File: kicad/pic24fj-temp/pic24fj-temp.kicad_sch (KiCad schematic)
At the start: 18 parts, among them Q1 BC328, Q2 BC328, Q3 BC328, Q4 BC328, U2 CA56-12CGKWA

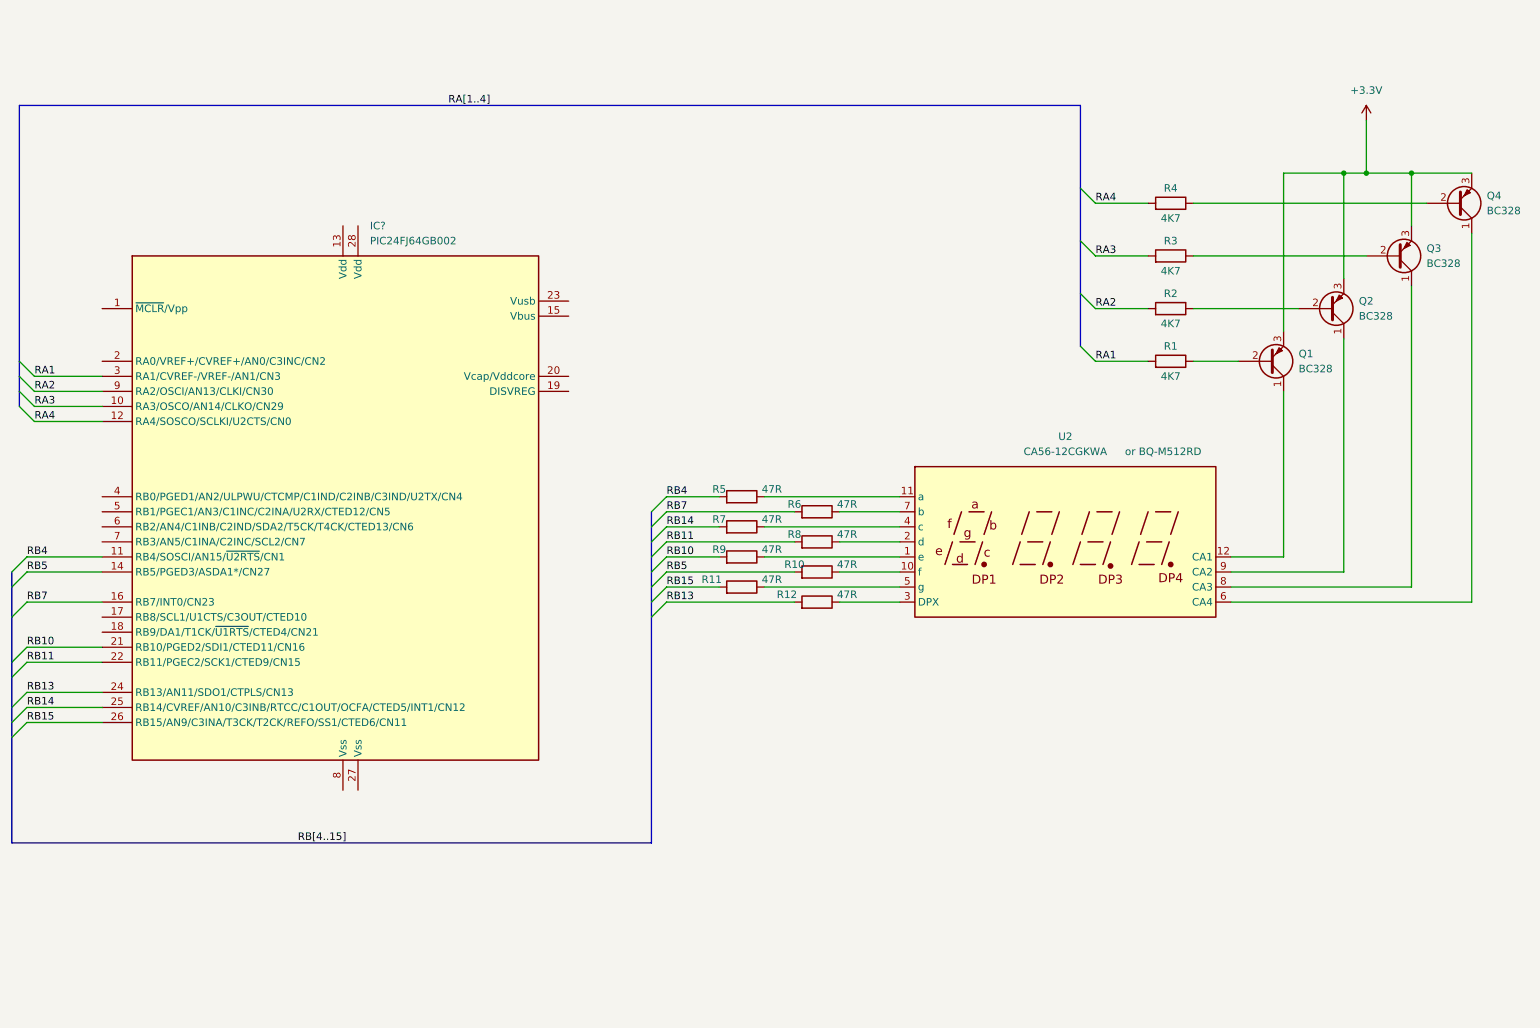
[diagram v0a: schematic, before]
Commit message: Added DS18B20 (no code yet), increased Mux freq from 100 Hz to 200 Hz to reduce flicker
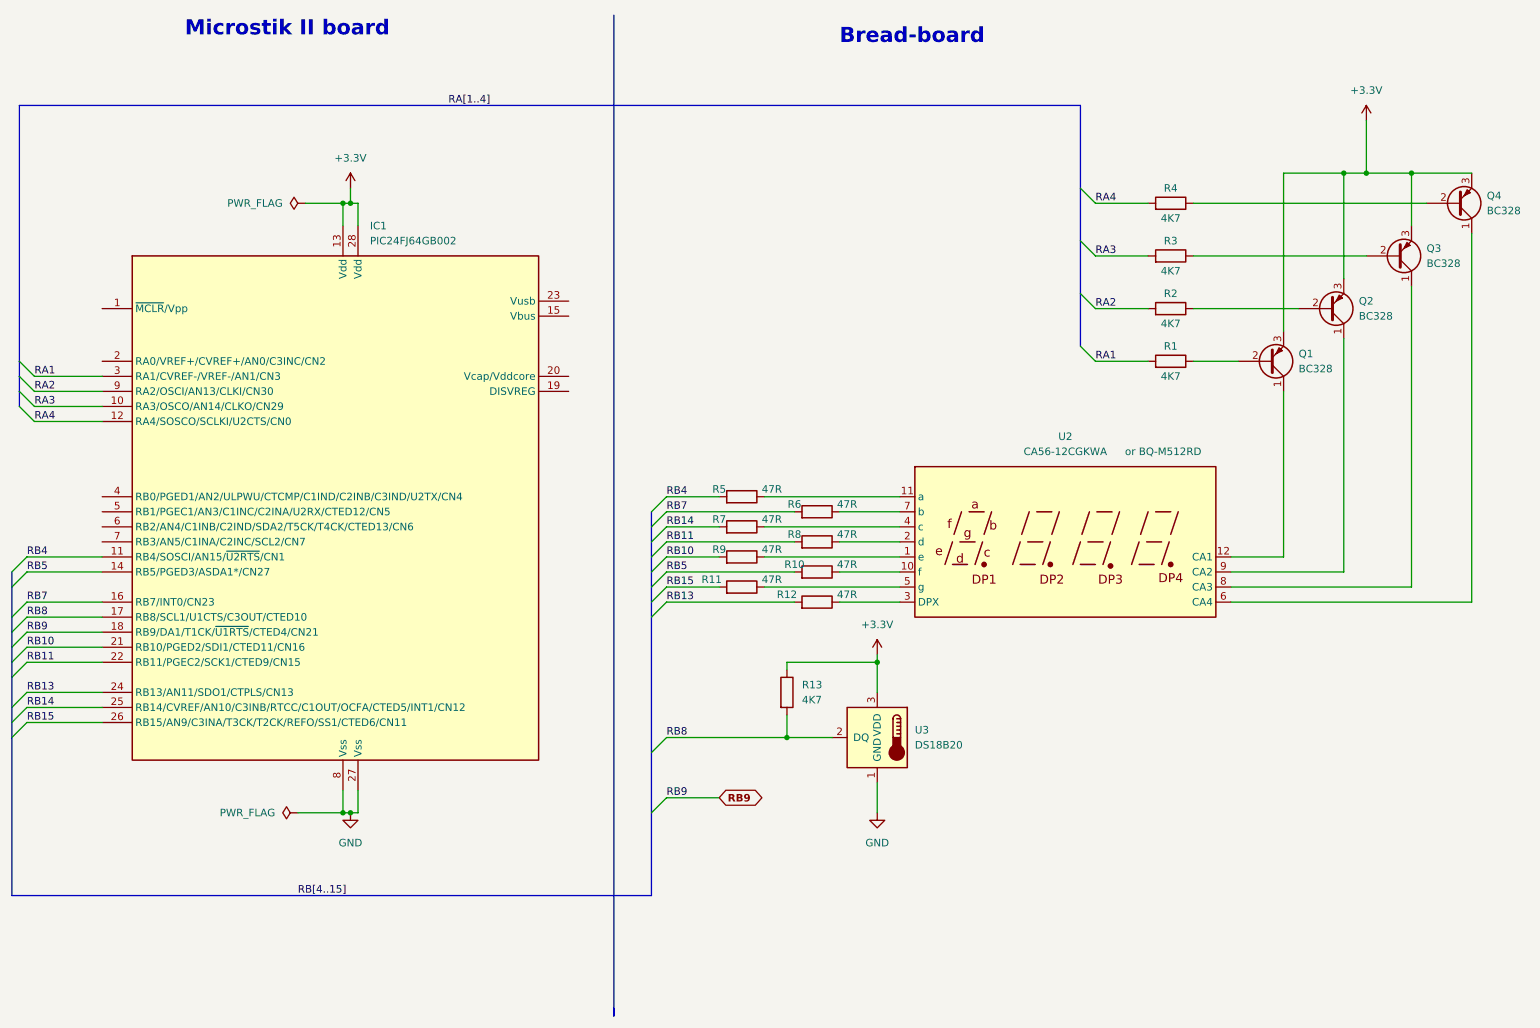
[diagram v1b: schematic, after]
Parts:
- added R13: 4K7, symbol Device:R
- added U3: DS18B20, Package_TO_SOT_THT:TO-92_Inline, symbol Sensor_Temperature:DS18B20
- gave numbers to parts that had none: 1
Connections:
- net +3.3V: now also IC1.13 (Vdd), IC1.28 (Vdd), R13.1, U3.3 (VDD)
- net RB8: now reaches IC1.17 (RB8/SCL1/U1CTS/C3OUT/CTED10)
- net RB8: now also R13.2, U3.2 (DQ)
- net RB9: now reaches IC1.18 (RB9/DA1/T1CK/~{U1RTS}/CTED4/CN21)
- net GND: now reaches IC1.27 (Vss)
- net GND: now also IC1.8 (Vss), U3.1 (GND)
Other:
- note added: "Bread-board"
- note added: "Microstik II board"
- title: PIC24FJ Temperatur meter with 4 digit LED display -> PIC24FJ Thermometer with DS18B20 and 4 digit LED display
